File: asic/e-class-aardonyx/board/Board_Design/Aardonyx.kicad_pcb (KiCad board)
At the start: 4 copper layers, 157.5 x 117.3 mm, 327 parts, among them J1 USB_B_6PIN, J10 Conn_1x6, J11 Conn_1x6, J12 Conn_1x3_M, J13 Conn_1x8_F, J14 Conn_1x6_F, J15 Conn_1x10_F, J16 Conn_1x8_F, J17 USB_OTG, J18 Conn_1x3_M, J19 Conn_1x3_M, J2 Conn_1x8, J3 Conn_1x3_M, J4 Conn_1x4, J5 PJ-202H PWRJACK, J6 Conn_1x3_M, J7 Conn_1x4, J8 Conn_1x3_M, J9 Conn_1x8, Q1 FDN339AN, SW1 SW_SPST, SW2 FSM2JSMAATR, SW3 SW_DIP_x03, U1 FT2232H, U10 TPS7A7002DDAR, U11 ADM1186, U13 TPS7A7002DDAR, U14 74AUP1G09GW, U15 SKT32E, U16 93LC56BT-I_OT, U2 IS42S32160F-TSOP2, U3 CDCE913PW, U4 TPS54627DDAR, U5 CAT24M01WI-GT3, U6 IS25LP256x-xM, U7 ADC128S102CIMTX/NOPB, U8 LSF0108PWR, U9 LSF0108PWR, Y1 12MHz, Y2 27MHz

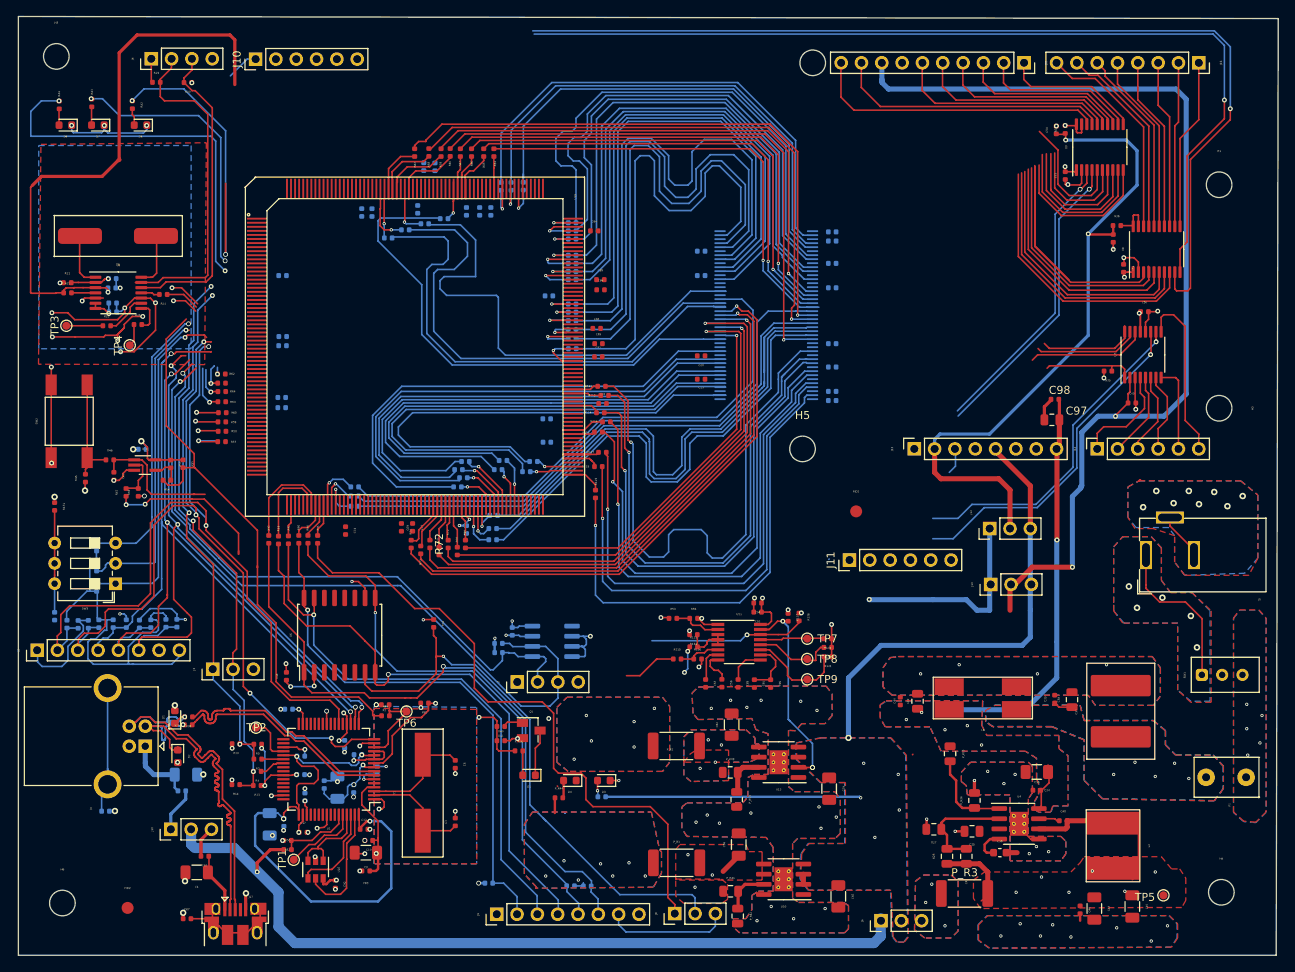
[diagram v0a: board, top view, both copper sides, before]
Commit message: updated tracks
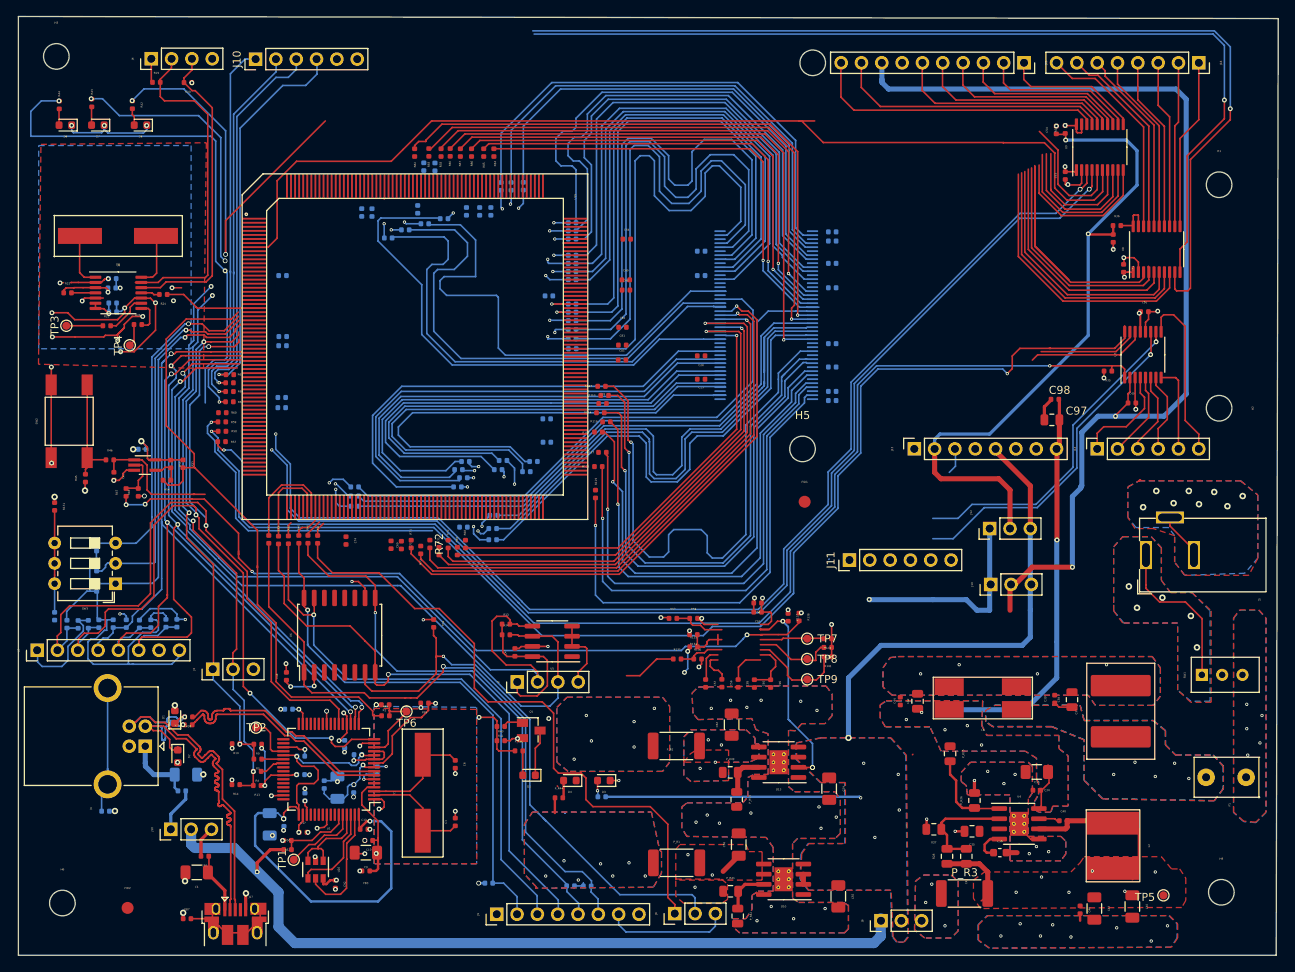
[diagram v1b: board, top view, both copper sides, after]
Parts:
- removed R21: 4.7KE,0402, Resistor_SMD:R_0402_1005Metric
- removed U11: ADM1186, Package_SO:QSOP-16_3.9x4.9mm_P0.635mm
- C47, R33, R34, U5: moved to F.Cu
- moved FID1 6.55 mm to (221.5, 105.9)
- moved C64 4.19 mm to (199.2, 73.0)
- moved R33 3.68 mm to (184.1, 121.2)
- moved C84 3.23 mm to (198.7, 84.1)
- moved C89 3.18 mm to (199.1, 78.1)
- moved C86 3.18 mm to (199.1, 79.4)
- moved C81 2.99 mm to (198.6, 88.2)
- moved C83 2.98 mm to (198.7, 86.3)
- moved C47 2.64 mm to (185.3, 124.7), turned to 90 degrees
- moved C77 2.62 mm to (171.1, 111.3)
- moved C69 2.53 mm to (169.8, 111.2)
- moved R34 1.43 mm to (184.1, 122.5)
- moved C74 1.25 mm to (164.1, 110.7)
- moved R62 1.06 mm to (149.6, 90.0)
- moved R61 0.99 mm to (149.6, 91.0)
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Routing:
- net /arduino_header/SPI0_CLK: track 15.4 -> 159.0 mm, vias 1 -> 2
- net /arduino_header/SPI0_nCS: track 16.9 -> 153.0 mm, vias 1 -> 2
- net /arduino_header/IO_12: track 14.2 -> 127.0 mm
- net /arduino_header/I2C1_SCL: track 37.0 -> 148.5 mm, vias 1 -> 2
- net /arduino_header/I2C1_SDA: track 37.7 -> 148.3 mm, vias 1 -> 2
- net V1P8: track 91.5 -> 19.7 mm, vias 13 -> 11
- net /power_2/RESET_ASIC: track 40.0 -> 97.5 mm, vias 3 -> 4
- net /arduino_header/SPI1_CLK: track 0.86 -> 47.8 mm
- net /arduino_header/SPI1_nCS: track 3.21 -> 47.4 mm
- net /arduino_header/SPI1_MOSI: track 3.96 -> 47.1 mm
- net /arduino_header/SPI1_MISO: track 9.68 -> 48.4 mm
- net /arduino_header/SPI0_MISO: track 16.0 -> 52.3 mm
- net /arduino_header/I2C0_SDA: track 80.0 -> 99.0 mm
- net /arduino_header/IO_15: track 47.3 -> 65.8 mm
- net V3P3: track 146.0 -> 160.2 mm, vias 46 -> 44
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
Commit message: Updating Layout
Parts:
- added R21: 4.7KE,0402, Resistor_SMD:R_0402_1005Metric, F.Cu at (129.6, 78.5)
- added U11: ADM1186, Package_SO:QSOP-16_3.9x4.9mm_P0.635mm, F.Cu at (213.3, 123.4)
- moved TP4 7.93 mm to (129.2, 86.2)
- moved R26 4.59 mm to (134.3, 86.2)
- moved C4 0.86 mm to (156.4, 146.8)
- moved R34 0.13 mm to (184.1, 122.6)
- moved R25 0.08 mm to (134.3, 83.9)
- turned C17 to 180 degrees
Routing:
- net GND: track 235.3 -> 267.6 mm, vias 113 -> 107
- net Net-(R26-Pad2): track 4.01 -> 8.01 mm
- net Net-(C35-Pad1): track 0.00 -> 2.59 mm
- net VCORE_FTDI: track 72.3 -> 74.7 mm
- net Net-(R21-Pad2): track 4.92 -> 6.96 mm
- net V1P8: track 19.7 -> 21.6 mm
- net Net-(R26-Pad1): track 2.81 -> 4.59 mm
- net V3P3: track 160.2 -> 162.0 mm, vias 44 -> 43
- net /arduino_header/I2C0_SCL: track 98.0 -> 96.7 mm
- net /arduino_header/I2C1_SCL: track 148.5 -> 149.5 mm
- net /arduino_header/I2C1_SDA: track 148.3 -> 148.9 mm
- net V5P0: vias 6 -> 5
- net Net-(C10-Pad1): vias 1 -> 0

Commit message: Updating layout
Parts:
- C48: moved to B.Cu
- R142, R30, R31: moved to F.Cu
- moved R30 47.4 mm to (156.7, 125.1)
- moved R142 43.6 mm to (160.4, 115.7), turned to 0 degrees
- moved R31 42.0 mm to (169.8, 118.3), turned to 90 degrees
- moved R32 6.56 mm to (169.8, 125.0), turned to 180 degrees
- moved R16 5.21 mm to (134.5, 120.8), turned to 180 degrees
- moved R11 4.76 mm to (131.9, 120.8), turned to 0 degrees
- moved C48 4.74 mm to (160.2, 124.5)
- moved R132 4.72 mm to (130.1, 116.1), turned to 180 degrees
- moved R18 4.64 mm to (137.1, 121.9), turned to 180 degrees
- moved R5 4.35 mm to (126.3, 120.7), turned to 0 degrees
- moved R15 3.95 mm to (134.5, 122.0), turned to 0 degrees
- moved R8 3.88 mm to (129.5, 122.0), turned to 180 degrees
- moved R17 3.32 mm to (139.8, 121.8), turned to 180 degrees
- moved R12 3.24 mm to (132.0, 122.1), turned to 180 degrees
- moved R6 3.01 mm to (126.3, 121.8), turned to 180 degrees
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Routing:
- net GND: track 267.6 -> 252.7 mm, vias 107 -> 133
- net V3P3: track 162.0 -> 175.5 mm, vias 43 -> 60
- net Net-(R78-Pad1): track 0.00 -> 9.86 mm
- net Net-(R80-Pad1): track 0.00 -> 9.37 mm
- net Net-(R83-Pad1): track 0.00 -> 9.03 mm
- net Net-(R82-Pad1): track 0.00 -> 7.32 mm
- net Net-(R73-Pad1): track 0.00 -> 7.23 mm
- net Net-(R74-Pad1): track 0.00 -> 6.95 mm
- net Net-(R71-Pad1): track 0.00 -> 6.86 mm
- net Net-(R69-Pad1): track 0.00 -> 6.72 mm
- net Net-(R85-Pad1): track 0.00 -> 6.26 mm
- net Net-(R72-Pad1): track 0.00 -> 6.23 mm
- net Net-(R68-Pad1): track 0.00 -> 5.84 mm
- net Net-(R86-Pad1): track 0.00 -> 5.74 mm
- net Net-(R70-Pad1): track 0.00 -> 5.71 mm
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
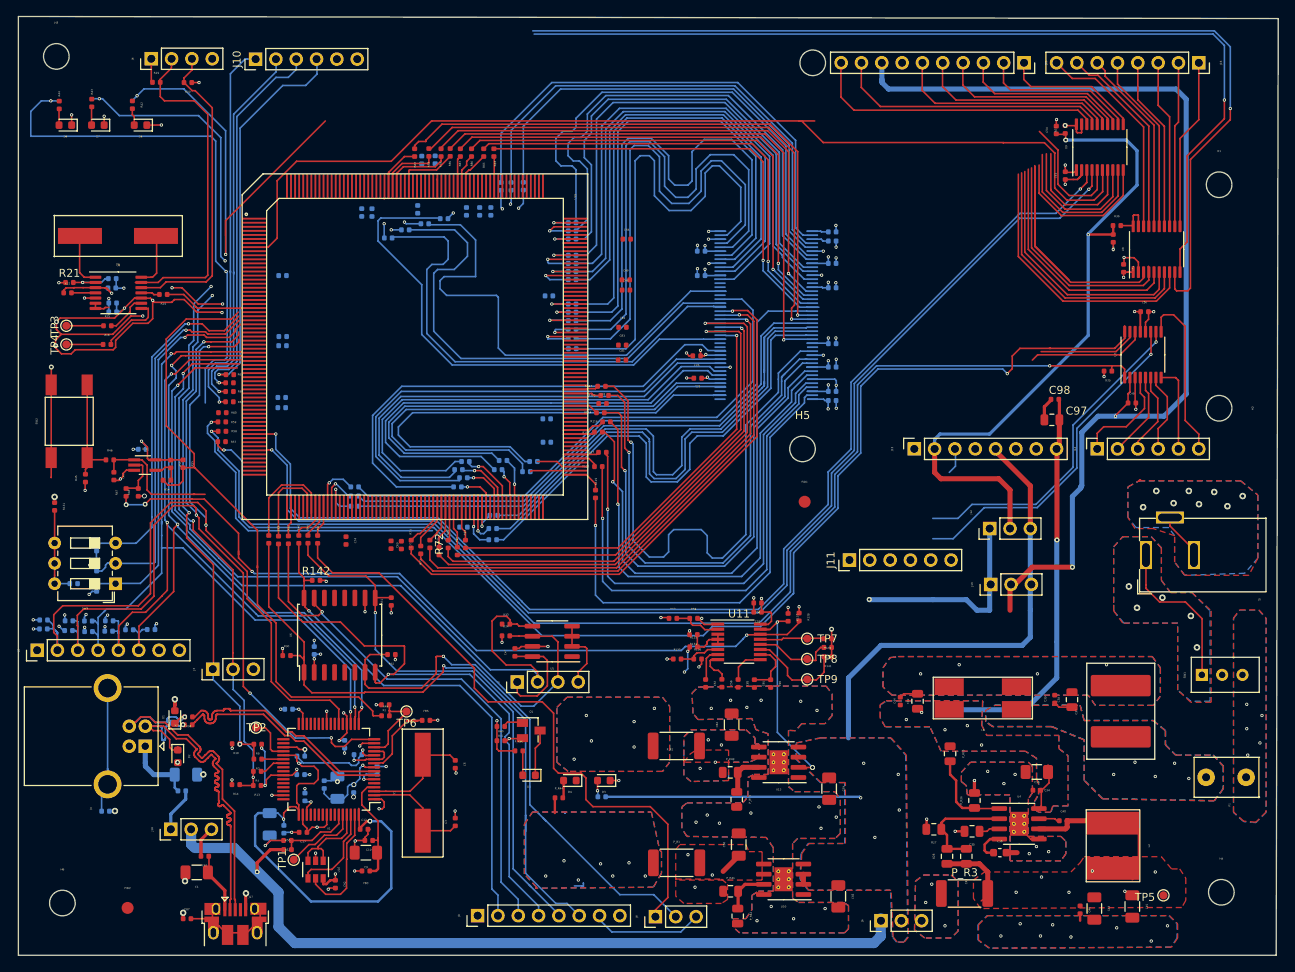
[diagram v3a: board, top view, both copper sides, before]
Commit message: updated footprint & tracks
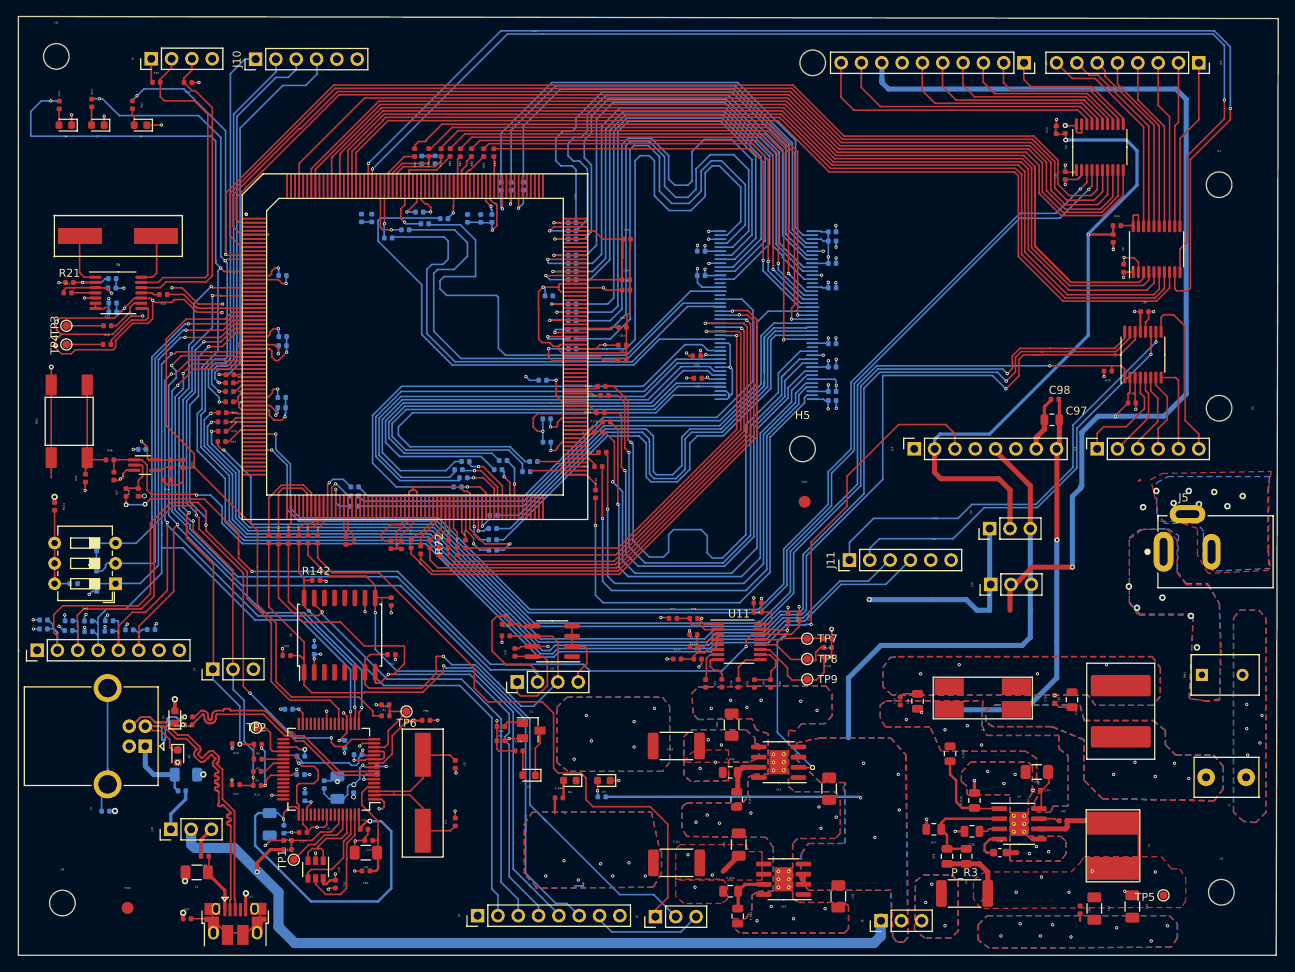
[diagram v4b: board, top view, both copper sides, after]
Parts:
- C78: moved to B.Cu
- J5: footprint Aardonyx:Pwr_Jack_DC_PJ-202AH_Horizontal -> Aardonyx:CUI_PJ-202AH
- moved J5 8.71 mm to (272.8, 112.1), turned to 0 degrees
- moved C78 8.05 mm to (188.7, 90.7), turned to 180 degrees
- moved C72 4.66 mm to (182.5, 111.9)
- moved C67 0.89 mm to (181.0, 70.5)
- moved C70 0.89 mm to (179.3, 70.5)
- moved C88 0.89 mm to (182.4, 70.5)
- moved C73 0.68 mm to (167.4, 70.4)
- moved C76 0.68 mm to (166.1, 70.4)
- moved C90 0.40 mm to (173.3, 69.7), turned to 0 degrees
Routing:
- net GND: track 252.7 -> 412.6 mm, vias 133 -> 144
- net /arduino_header/SPI0_MOSI: track 14.9 -> 166.5 mm, vias 0 -> 2
- net /arduino_header/IO_14: track 33.9 -> 169.3 mm
- net /arduino_header/RESET_AH: track 20.5 -> 143.2 mm, vias 0 -> 2
- net /arduino_header/IO_11: track 16.0 -> 135.3 mm
- net /arduino_header/IO_15: track 65.8 -> 184.1 mm
- net /arduino_header/IO_10: track 17.8 -> 133.6 mm
- net /arduino_header/SPI0_MISO: track 52.3 -> 162.7 mm, vias 1 -> 2
- net /arduino_header/IO_9: track 19.3 -> 122.3 mm
- net /arduino_header/IO_8: track 19.4 -> 120.9 mm
- net /arduino_header/IO_7: track 42.4 -> 142.7 mm
- net /arduino_header/IO_13: track 67.9 -> 167.6 mm
- net /arduino_header/IO_6: track 28.0 -> 126.4 mm
- net /arduino_header/IO_5: track 29.6 -> 126.4 mm
- net /arduino_header/IO_4: track 31.5 -> 127.0 mm
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
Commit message: Updating layout
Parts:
- C60, R31, R32, R46, R47, R48, R51, R54, R55, U14: moved to B.Cu
- moved FID1 63.0 mm to (275.0, 72.6)
- moved R48 14.0 mm to (129.5, 93.8), turned to 270 degrees
- moved R55 13.1 mm to (134.0, 92.3), turned to 0 degrees
- moved C53 13.0 mm to (241.1, 65.2)
- moved C54 13.0 mm to (240.0, 59.5)
- moved U9 13.0 mm to (245.4, 61.7)
- moved R37 13.0 mm to (241.1, 59.5)
- moved C98 12.2 mm to (251.7, 105.2)
- moved R47 11.8 mm to (128.7, 95.9)
- moved R54 11.5 mm to (136.4, 93.0), turned to 90 degrees
- moved R51 11.1 mm to (134.0, 93.6), turned to 0 degrees
- moved C48 8.75 mm to (168.9, 125.2)
- moved U6 8.67 mm to (172.0, 123.3)
- moved R30 8.42 mm to (165.0, 126.6)
- moved C60 7.75 mm to (130.3, 96.6), turned to 90 degrees
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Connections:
- J11 pad 1: /arduino_header/A6 -> V3P3
- J11 pad 2: /arduino_header/A7 -> /arduino_header/IO_14
- J11 pad 3: /arduino_header/IO_14 -> /arduino_header/IO_15
- J11 pad 4: /arduino_header/IO_15 -> /arduino_header/A6
- J11 pad 5: V3P3 -> /arduino_header/A7
- J2 pad 2: /ftdi/TRST -> /ftdi/TCK
- J2 pad 3: /ftdi/TCK -> /ftdi/TRST
- J2 pad 5: /soc/TD0 -> /ftdi/TDI
- J2 pad 6: /ftdi/TDI -> /soc/TD0
- J7 pad 2: /arduino_header/I2C0_SDA -> /arduino_header/I2C0_SCL
- J7 pad 3: /arduino_header/I2C0_SCL -> /arduino_header/I2C0_SDA
- R15 pad 2: /soc/TD0 -> /ftdi/TDI
- R16 pad 1: /soc/TD0 -> /ftdi/TDI
- R17 pad 2: /ftdi/TDI -> /soc/TD0
- R18 pad 1: /ftdi/TDI -> /soc/TD0
- R5 pad 2: /ftdi/TRST -> /ftdi/TCK
- R6 pad 1: /ftdi/TRST -> /ftdi/TCK
- R7 pad 2: /ftdi/TCK -> /ftdi/TRST
- R8 pad 1: /ftdi/TCK -> /ftdi/TRST
- U10 pad 1: Net-(U10-Pad1) -> GND
- U10 pad 4: Net-(U10-Pad4) -> V5P0
- U10 pad 5: Net-(U10-Pad5) -> Net-(C56-Pad1)
- U13 pad 1: Net-(U13-Pad1) -> GND
- U13 pad 4: Net-(U13-Pad4) -> V5P0
- U13 pad 5: Net-(U13-Pad5) -> Net-(C62-Pad1)
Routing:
- net V1P8: track 83.4 -> 332.4 mm, vias 13 -> 28
- net GND: track 412.6 -> 357.9 mm, vias 144 -> 175
- net V3P3: track 226.5 -> 195.7 mm, vias 68 -> 71
- net /arduino_header/IO_1: track 156.7 -> 126.0 mm
- net /arduino_header/IO_7: track 142.7 -> 115.4 mm
- net /arduino_header/IO_0: track 148.4 -> 127.4 mm
- net /power_2/RESET_ASIC: track 100.3 -> 119.7 mm, vias 4 -> 3
- net /arduino_header/IO_13: track 167.6 -> 150.9 mm
- net /arduino_header/IO_11: track 135.3 -> 118.7 mm
- net /arduino_header/IO_12: track 135.9 -> 120.2 mm
- net /arduino_header/IO_15: track 184.1 -> 168.9 mm
- net /arduino_header/I2C0_SDA: track 101.9 -> 87.6 mm, vias 1 -> 2
- net /arduino_header/IO_10: track 133.6 -> 119.6 mm
- net VAC: track 130.1 -> 116.3 mm
- net /soc/TD0: track 95.8 -> 83.1 mm, vias 3 -> 2
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- added copper zone on B.Cu, net Net-(C56-Pad1)
- added copper zone on In2.Cu, net Net-(C56-Pad1)
- added copper zone on In2.Cu, net Net-(C62-Pad1)
- added copper zone on In2.Cu, net V1P8
- added copper zone on B.Cu, net VCC5V
- removed copper zone on In2.Cu, net Net-(J6-Pad1)
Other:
- rule trace_min: 0.2032 -> 0
